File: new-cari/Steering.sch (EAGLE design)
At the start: 19 parts, among them J1 UX60-MB-5S8, J2 AVR_SPI_PROG_3X2TESTPOINTS, X1 TSX-3225 16.0000MF18X-AC0

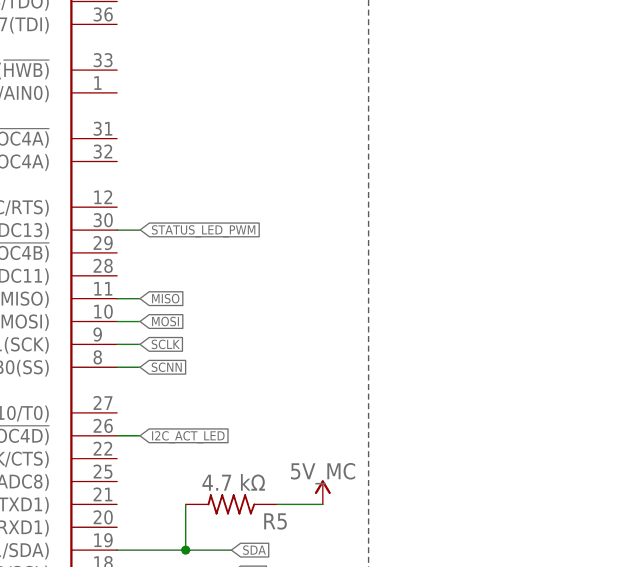
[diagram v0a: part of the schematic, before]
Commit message: Update Steering.sch
cleaned up and labeled some stuff
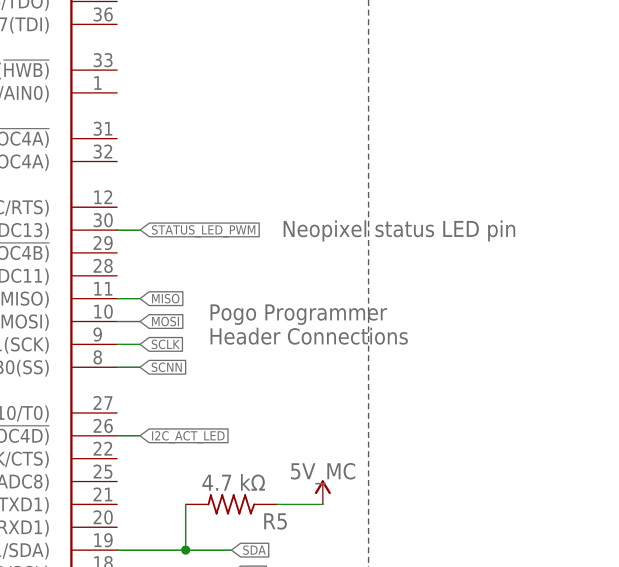
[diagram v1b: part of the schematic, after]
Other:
- note added: "Neopixel status LED pin"
- note added: "Pogo Programmer Header Connections"
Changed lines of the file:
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@@
 NEED PLACEMENT</text>
 <text x="40.64" y="170.18" size="1.778" layer="95">REPLACE THE SWITCH</text>
+<text x="246.38" y="162.56" size="1.778" layer="95">Pogo Programmer
+Header Connections</text>
+<text x="254.508" y="174.498" size="1.778" layer="95">Neopixel status LED pin</text>
 </plain>
 <instances>

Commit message: Added some notes
Added some notes
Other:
- note added: "Add in a PISO shift register to read the stepper feedback pins. Might also need level shifter"
- note added: "Stepper Feedback"
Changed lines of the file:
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@@
 Header Connections</text>
 <text x="254.508" y="174.498" size="1.778" layer="95">Neopixel status LED pin</text>
+<wire x1="298.958" y1="259.04" x2="298.958" y2="226.02" width="0.1524" layer="97" style="shortdash"/>
+<wire x1="298.958" y1="226.02" x2="349.758" y2="226.02" width="0.1524" layer="97" style="shortdash"/>
+<wire x1="349.758" y1="226.02" x2="349.758" y2="259.04" width="0.1524" layer="97" style="shortdash"/>
+<wire x1="349.758" y1="259.04" x2="298.958" y2="259.04" width="0.1524" layer="97" style="shortdash"/>
+<text x="301.498" y="255.23" size="1.778" layer="97">Stepper Feedback</text>
+<text x="307.34" y="238.76" size="1.778" layer="91">Add in a PISO shift register
+to read the stepper feedback pins.
+Might also need level shifter</text>
 </plain>
 <instances>
